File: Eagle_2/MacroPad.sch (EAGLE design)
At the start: 40 parts, among them SW00 SWITCH-SMD-SCHURTER-1241.1612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, SW01 KEYSWITCH-PLAIN-MX-1U, SW02 KEYSWITCH-PLAIN-MX-1U, SW03 KEYSWITCH-PLAIN-MX-1U, SW04 KEYSWITCH-PLAIN-MX-1U, SW05 KEYSWITCH-PLAIN-MX-1U, SW06 KEYSWITCH-PLAIN-MX-1U, SW07 KEYSWITCH-PLAIN-MX-1U, SW08 KEYSWITCH-PLAIN-MX-1U, SW09 KEYSWITCH-PLAIN-MX-1U, SW10 KEYSWITCH-PLAIN-MX-1U, SW11 KEYSWITCH-PLAIN-MX-1U, SW12 KEYSWITCH-PLAIN-MX-1U

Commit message: Create schematic and start aligning pin order
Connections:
- net N$10: now also U$1.PD6(RTS); no longer U$1.PD2(RX)
- net N$16: now also U$1.PD4; no longer U$1.PD0
- net N$26: now also U$1.PD2(RX); no longer U$1.PD4
- net N$32: now also U$1.PD1; no longer U$1.PD5
- net N$38: now also U$1.PD0; no longer U$1.PD6(RTS)
- net N$40: now also U$1.PD5; no longer U$1.PD1
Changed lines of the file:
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@@
 <pinref part="SW01" gate="G$1" pin="P0"/>
 <wire x1="170.18" y1="124.46" x2="172.72" y2="124.46" width="0.1524" layer="91"/>
-<wire x1="172.72" y1="124.46" x2="172.72" y2="137.16" width="0.1524" layer="91"/>
+<wire x1="172.72" y1="124.46" x2="172.72" y2="147.32" width="0.1524" layer="91"/>
 <pinref part="SW04" gate="G$1" pin="P0"/>
 <wire x1="170.18" y1="86.36" x2="172.72" y2="86.36" width="0.1524" layer="91"/>
@@
 <wire x1="172.72" y1="48.26" x2="172.72" y2="10.16" width="0.1524" layer="91"/>
 <junction x="172.72" y="48.26"/>
-<pinref part="U$1" gate="G$1" pin="PD2(RX)"/>
-<wire x1="93.98" y1="55.88" x2="129.54" y2="55.88" width="0.1524" layer="91"/>
-<wire x1="129.54" y1="55.88" x2="129.54" y2="137.16" width="0.1524" layer="91"/>
-<wire x1="129.54" y1="137.16" x2="172.72" y2="137.16" width="0.1524" layer="91"/>
+<pinref part="U$1" gate="G$1" pin="PD6(RTS)"/>
+<wire x1="93.98" y1="45.72" x2="144.78" y2="45.72" width="0.1524" layer="91"/>
+<wire x1="144.78" y1="45.72" x2="144.78" y2="147.32" width="0.1524" layer="91"/>
+<wire x1="144.78" y1="147.32" x2="172.72" y2="147.32" width="0.1524" layer="91"/>
 </segment>
 </net>
@@
 <wire x1="180.34" y1="101.6" x2="157.48" y2="101.6" width="0.1524" layer="91"/>
 <junction x="157.48" y="101.6"/>
-<wire x1="157.48" y1="101.6" x2="132.08" y2="101.6" width="0.1524" layer="91"/>
+<wire x1="157.48" y1="101.6" x2="137.16" y2="101.6" width="0.1524" layer="91"/>
 <junction x="180.34" y="101.6"/>
-<wire x1="132.08" y1="101.6" x2="132.08" y2="53.34" width="0.1524" layer="91"/>
 <pinref part="U$1" gate="G$1" pin="PD3(TX)"/>
-<wire x1="132.08" y1="53.34" x2="93.98" y2="53.34" width="0.1524" layer="91"/>
+<wire x1="93.98" y1="53.34" x2="137.16" y2="53.34" width="0.1524" layer="91"/>
+<wire x1="137.16" y1="53.34" x2="137.16" y2="101.6" width="0.1524" layer="91"/>
 </segment>
 </net>
@@
 <pinref part="SW03" gate="G$1" pin="P0"/>
 <wire x1="215.9" y1="124.46" x2="218.44" y2="124.46" width="0.1524" layer="91"/>
-<wire x1="218.44" y1="124.46" x2="218.44" y2="142.24" width="0.1524" layer="91"/>
+<wire x1="218.44" y1="124.46" x2="218.44" y2="152.4" width="0.1524" layer="91"/>
 <pinref part="SW06" gate="G$1" pin="P0"/>
 <wire x1="215.9" y1="86.36" x2="218.44" y2="86.36" width="0.1524" layer="91"/>
@@
 <wire x1="218.44" y1="48.26" x2="218.44" y2="10.16" width="0.1524" layer="91"/>
 <junction x="218.44" y="48.26"/>
-<pinref part="U$1" gate="G$1" pin="PD0"/>
-<wire x1="93.98" y1="60.96" x2="124.46" y2="60.96" width="0.1524" layer="91"/>
-<wire x1="124.46" y1="60.96" x2="124.46" y2="142.24" width="0.1524" layer="91"/>
-<wire x1="124.46" y1="142.24" x2="218.44" y2="142.24" width="0.1524" layer="91"/>
+<pinref part="U$1" gate="G$1" pin="PD4"/>
+<wire x1="93.98" y1="50.8" x2="139.7" y2="50.8" width="0.1524" layer="91"/>
+<wire x1="139.7" y1="50.8" x2="139.7" y2="152.4" width="0.1524" layer="91"/>
+<wire x1="139.7" y1="152.4" x2="218.44" y2="152.4" width="0.1524" layer="91"/>
 </segment>
 </net>
@@
 <junction x="157.48" y="63.5"/>
 <wire x1="157.48" y1="63.5" x2="134.62" y2="63.5" width="0.1524" layer="91"/>
-<wire x1="134.62" y1="63.5" x2="134.62" y2="50.8" width="0.1524" layer="91"/>
-<pinref part="U$1" gate="G$1" pin="PD4"/>
-<wire x1="134.62" y1="50.8" x2="93.98" y2="50.8" width="0.1524" layer="91"/>
+<wire x1="134.62" y1="63.5" x2="134.62" y2="55.88" width="0.1524" layer="91"/>
+<pinref part="U$1" gate="G$1" pin="PD2(RX)"/>
+<wire x1="134.62" y1="55.88" x2="93.98" y2="55.88" width="0.1524" layer="91"/>
 </segment>
 </net>
@@
 <junction x="157.48" y="25.4"/>
 <wire x1="157.48" y1="25.4" x2="132.08" y2="25.4" width="0.1524" layer="91"/>
-<wire x1="132.08" y1="25.4" x2="132.08" y2="48.26" width="0.1524" layer="91"/>
-<pinref part="U$1" gate="G$1" pin="PD5"/>
-<wire x1="132.08" y1="48.26" x2="93.98" y2="48.26" width="0.1524" layer="91"/>
+<wire x1="132.08" y1="25.4" x2="132.08" y2="58.42" width="0.1524" layer="91"/>
+<pinref part="U$1" gate="G$1" pin="PD1"/>
+<wire x1="132.08" y1="58.42" x2="93.98" y2="58.42" width="0.1524" layer="91"/>
 </segment>
 </net>
@@
 <junction x="180.34" y="-12.7"/>
 <wire x1="157.48" y1="-12.7" x2="129.54" y2="-12.7" width="0.1524" layer="91"/>
-<pinref part="U$1" gate="G$1" pin="PD6(RTS)"/>
-<wire x1="93.98" y1="45.72" x2="129.54" y2="45.72" width="0.1524" layer="91"/>
-<wire x1="129.54" y1="45.72" x2="129.54" y2="-12.7" width="0.1524" layer="91"/>
+<pinref part="U$1" gate="G$1" pin="PD0"/>
+<wire x1="93.98" y1="60.96" x2="129.54" y2="60.96" width="0.1524" layer="91"/>
+<wire x1="129.54" y1="60.96" x2="129.54" y2="-12.7" width="0.1524" layer="91"/>
 </segment>
 </net>
@@
 <pinref part="SW02" gate="G$1" pin="P0"/>
 <wire x1="193.04" y1="124.46" x2="195.58" y2="124.46" width="0.1524" layer="91"/>
-<wire x1="195.58" y1="124.46" x2="195.58" y2="139.7" width="0.1524" layer="91"/>
+<wire x1="195.58" y1="124.46" x2="195.58" y2="149.86" width="0.1524" layer="91"/>
 <pinref part="SW05" gate="G$1" pin="P0"/>
 <wire x1="193.04" y1="86.36" x2="195.58" y2="86.36" width="0.1524" layer="91"/>
@@
 <wire x1="195.58" y1="10.16" x2="195.58" y2="48.26" width="0.1524" layer="91"/>
 <junction x="195.58" y="48.26"/>
-<wire x1="195.58" y1="139.7" x2="127" y2="139.7" width="0.1524" layer="91"/>
-<wire x1="127" y1="139.7" x2="127" y2="58.42" width="0.1524" layer="91"/>
-<pinref part="U$1" gate="G$1" pin="PD1"/>
-<wire x1="127" y1="58.42" x2="93.98" y2="58.42" width="0.1524" layer="91"/>
-</segment>
-</net>
+<wire x1="195.58" y1="149.86" x2="142.24" y2="149.86" width="0.1524" layer="91"/>
+<pinref part="U$1" gate="G$1" pin="PD5"/>
+<wire x1="142.24" y1="149.86" x2="142.24" y2="48.26" width="0.1524" layer="91"/>
+<wire x1="142.24" y1="48.26" x2="93.98" y2="48.26" width="0.1524" layer="91"/>
+</segment>
+</net>

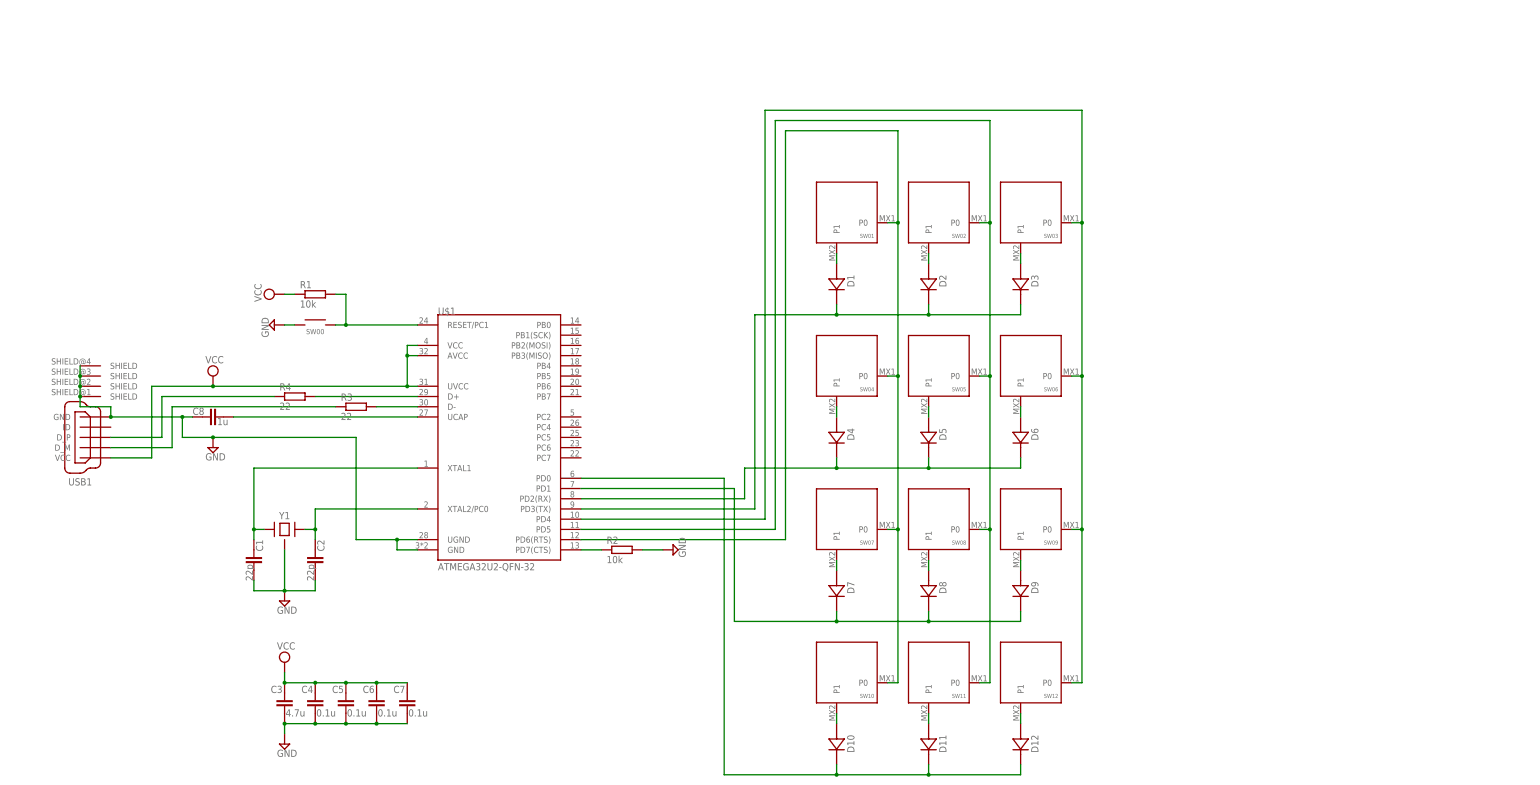
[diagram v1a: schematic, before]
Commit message: Update switch and chip footprints, and switch array pins
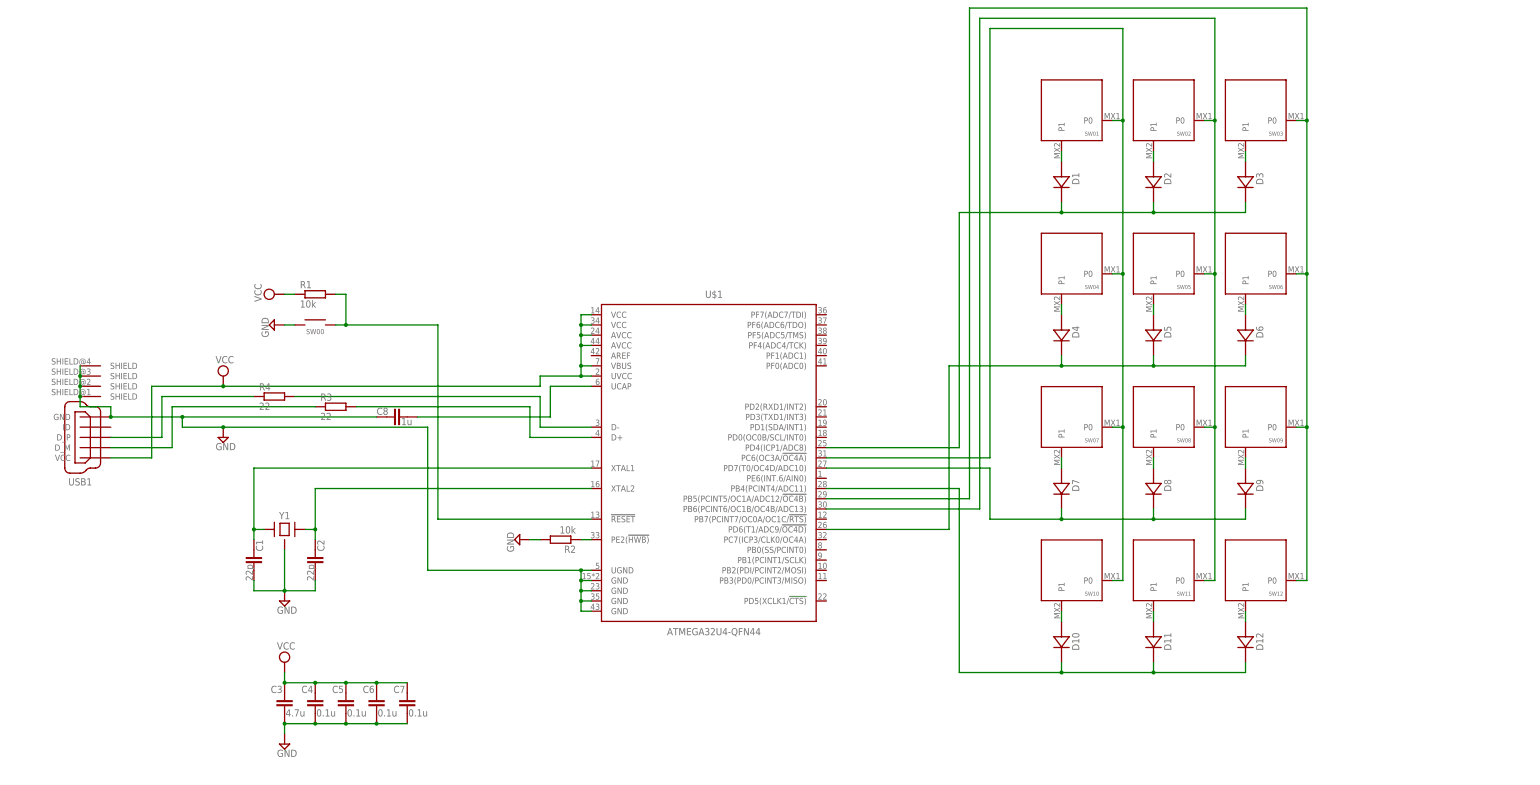
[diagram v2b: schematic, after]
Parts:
- SW00: value SWITCH-SMD-SCHURTER-1241.1612.11 -> SWITCH-SMD-EVQP-P2602W; device Hardware:SWITCH-SMD-SCHURTER-1241.1612.11 -> Hardware:SWITCH-SMD-EVQP-P2602W
- U$1: value ATMEGA32U2-QFN-32 -> ATMEGA32U4-QFN44; device Controller:ATMEGA32U2-QFN-32 -> Controller:ATMEGA32U4-QFN44
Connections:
- net GND: now also R2.2, U$1.GND@15, U$1.GND@23, U$1.GND@35, U$1.GND@43; no longer U$1.GND
- net N$1: now also U$1.XTAL2; no longer U$1.XTAL2/PC0
- net N$10: now also U$1.PC6(OC3A/!OC4A); no longer U$1.PD6(RTS)
- net N$14: now also U$1.PD4(ICP1/ADC8); no longer U$1.PD3(TX)
- net N$16: now also U$1.PB5(PCINT5/OC1A/ADC12/!OC4B); no longer U$1.PD4
- net N$26: now also U$1.PD6(T1/ADC9/!OC4D); no longer U$1.PD2(RX)
- net N$3: now also U$1.!RESET; no longer U$1.RESET/PC1
- net N$32: now also U$1.PD7(T0/OC4D/ADC10); no longer U$1.PD1
- net N$38: now also U$1.PB4(PCINT4/ADC11); no longer U$1.PD0
- net N$4: now also U$1.PE2(!HWB); no longer U$1.PD7(CTS)
- net N$40: now also U$1.PB6(PCINT6/OC1B/OC4B/ADC13); no longer U$1.PD5
- net N$6: now also U$1.D-; no longer U$1.D+
- net N$8: now also U$1.D+; no longer U$1.D-
- net UGND: no longer R2.2
- net VCC: now also U$1.AVCC@24, U$1.AVCC@44, U$1.VBUS, U$1.VCC@14, U$1.VCC@34; no longer U$1.AVCC, U$1.VCC
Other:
- moved on the sheet: C8, D1, D10, D11, D12, D2, D3, D4, D5, D6, D7, D8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

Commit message: Routed board
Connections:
- removed net GND: C8.1, R2.2, U$1.GND@15, U$1.GND@23, U$1.GND@35, U$1.GND@43, U$1.UGND, USB1.GND, USB1.SHIELD@1, USB1.SHIELD@2, USB1.SHIELD@3, USB1.SHIELD@4
- net UGND: now also C8.1, R2.2, U$1.GND@15, U$1.GND@23, U$1.GND@35, U$1.GND@43, U$1.UGND, USB1.GND, USB1.SHIELD@1, USB1.SHIELD@2, USB1.SHIELD@3, USB1.SHIELD@4
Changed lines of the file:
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@@
 <part name="U$1" library="Controller" deviceset="ATMEGA32U4" device="-QFN44"/>
 <part name="SW00" library="Hardware" deviceset="SWITCH-SMD" device="-EVQP-P2602W"/>
+<part name="SUPPLY9" library="supply2" library_urn="urn:adsk.eagle:library:372" deviceset="GND" device=""/>
 </parts>
 <sheets>
@@
 <instance part="SW00" gate="G$1" x="27.94" y="99.06" smashed="yes">
 <attribute name="NAME" x="27.94" y="96.774" size="1.27" layer="95" align="bottom-center"/>
+</instance>
+<instance part="SUPPLY9" gate="GND" x="66.04" y="17.78" smashed="yes">
+<attribute name="VALUE" x="64.135" y="14.605" size="1.778" layer="96"/>
 </instance>
 </instances>
@@
 <wire x1="20.32" y1="99.06" x2="22.86" y2="99.06" width="0.1524" layer="91"/>
 <pinref part="SW00" gate="G$1" pin="1"/>
+</segment>
+<segment>
+<pinref part="SUPPLY6" gate="GND" pin="GND"/>
+<pinref part="R2" gate="G$1" pin="2"/>
+<wire x1="81.28" y1="45.72" x2="83.82" y2="45.72" width="0.1524" layer="91"/>
+</segment>
+<segment>
+<pinref part="USB1" gate="G$1" pin="GND"/>
+<wire x1="-22.86" y1="76.2" x2="-5.08" y2="76.2" width="0.1524" layer="91"/>
+<wire x1="-5.08" y1="76.2" x2="43.18" y2="76.2" width="0.1524" layer="91"/>
+<wire x1="-22.86" y1="76.2" x2="-22.86" y2="78.74" width="0.1524" layer="91"/>
+<junction x="-22.86" y="76.2"/>
+<pinref part="USB1" gate="G$1" pin="SHIELD@2"/>
+<pinref part="USB1" gate="G$1" pin="SHIELD@1"/>
+<wire x1="-30.48" y1="83.82" x2="-30.48" y2="81.28" width="0.1524" layer="91"/>
+<pinref part="USB1" gate="G$1" pin="SHIELD@4"/>
+<pinref part="USB1" gate="G$1" pin="SHIELD@3"/>
+<wire x1="-30.48" y1="88.9" x2="-30.48" y2="86.36" width="0.1524" layer="91"/>
+<wire x1="-30.48" y1="83.82" x2="-30.48" y2="86.36" width="0.1524" layer="91"/>
+<junction x="-30.48" y="83.82"/>
+<junction x="-30.48" y="86.36"/>
+<wire x1="-22.86" y1="78.74" x2="-30.48" y2="78.74" width="0.1524" layer="91"/>
+<wire x1="-30.48" y1="78.74" x2="-30.48" y2="81.28" width="0.1524" layer="91"/>
+<junction x="-30.48" y="81.28"/>
+<pinref part="C8" gate="G$1" pin="1"/>
+<wire x1="-5.08" y1="76.2" x2="-5.08" y2="73.66" width="0.1524" layer="91"/>
+<junction x="-5.08" y="76.2"/>
+<wire x1="-5.08" y1="73.66" x2="5.08" y2="73.66" width="0.1524" layer="91"/>
+<wire x1="5.08" y1="73.66" x2="55.88" y2="73.66" width="0.1524" layer="91"/>
+<pinref part="SUPPLY7" gate="GND" pin="GND"/>
+<junction x="5.08" y="73.66"/>
+<pinref part="U$1" gate="G$1" pin="GND@43"/>
+<wire x1="96.52" y1="27.94" x2="93.98" y2="27.94" width="0.1524" layer="91"/>
+<wire x1="93.98" y1="27.94" x2="93.98" y2="30.48" width="0.1524" layer="91"/>
+<pinref part="U$1" gate="G$1" pin="GND@35"/>
+<wire x1="96.52" y1="30.48" x2="93.98" y2="30.48" width="0.1524" layer="91"/>
+<junction x="93.98" y="30.48"/>
+<wire x1="93.98" y1="30.48" x2="93.98" y2="33.02" width="0.1524" layer="91"/>
+<pinref part="U$1" gate="G$1" pin="GND@23"/>
+<wire x1="96.52" y1="33.02" x2="93.98" y2="33.02" width="0.1524" layer="91"/>
+<junction x="93.98" y="33.02"/>
+<wire x1="93.98" y1="33.02" x2="93.98" y2="35.56" width="0.1524" layer="91"/>
+<pinref part="U$1" gate="G$1" pin="GND@15"/>
+<wire x1="96.52" y1="35.56" x2="93.98" y2="35.56" width="0.1524" layer="91"/>
+<junction x="93.98" y="35.56"/>
+<wire x1="93.98" y1="35.56" x2="93.98" y2="38.1" width="0.1524" layer="91"/>
+<wire x1="93.98" y1="38.1" x2="55.88" y2="38.1" width="0.1524" layer="91"/>
+<wire x1="55.88" y1="73.66" x2="55.88" y2="38.1" width="0.1524" layer="91"/>
+<pinref part="U$1" gate="G$1" pin="UGND"/>
+<wire x1="96.52" y1="38.1" x2="93.98" y2="38.1" width="0.1524" layer="91"/>
+<junction x="93.98" y="38.1"/>
+</segment>
+<segment>
+<pinref part="SUPPLY9" gate="GND" pin="GND"/>
+<wire x1="66.04" y1="20.32" x2="66.04" y2="27.94" width="0.1524" layer="91"/>
+<label x="66.04" y="27.94" size="1.778" layer="95" xref="yes"/>
 </segment>
 </net>
@@
 </segment>
 </net>
-<net name="GND" class="0">
-<segment>
-<pinref part="USB1" gate="G$1" pin="GND"/>
-<wire x1="-22.86" y1="76.2" x2="-5.08" y2="76.2" width="0.1524" layer="91"/>
-<wire x1="-5.08" y1="76.2" x2="43.18" y2="76.2" width="0.1524" layer="91"/>
-<wire x1="-22.86" y1="76.2" x2="-22.86" y2="78.74" width="0.1524" layer="91"/>
-<junction x="-22.86" y="76.2"/>
-<pinref part="USB1" gate="G$1" pin="SHIELD@2"/>
-<pinref part="USB1" gate="G$1" pin="SHIELD@1"/>
-<wire x1="-30.48" y1="83.82" x2="-30.48" y2="81.28" width="0.1524" layer="91"/>
-<pinref part="USB1" gate="G$1" pin="SHIELD@4"/>
-<pinref part="USB1" gate="G$1" pin="SHIELD@3"/>
-<wire x1="-30.48" y1="88.9" x2="-30.48" y2="86.36" width="0.1524" layer="91"/>
-<wire x1="-30.48" y1="83.82" x2="-30.48" y2="86.36" width="0.1524" layer="91"/>
-<junction x="-30.48" y="83.82"/>
-<junction x="-30.48" y="86.36"/>
-<wire x1="-22.86" y1="78.74" x2="-30.48" y2="78.74" width="0.1524" layer="91"/>
-<wire x1="-30.48" y1="78.74" x2="-30.48" y2="81.28" width="0.1524" layer="91"/>
-<junction x="-30.48" y="81.28"/>
-<pinref part="C8" gate="G$1" pin="1"/>
-<wire x1="-5.08" y1="76.2" x2="-5.08" y2="73.66" width="0.1524" layer="91"/>
-<junction x="-5.08" y="76.2"/>
-<wire x1="-5.08" y1="73.66" x2="5.08" y2="73.66" width="0.1524" layer="91"/>
-<wire x1="5.08" y1="73.66" x2="55.88" y2="73.66" width="0.1524" layer="91"/>
-<pinref part="SUPPLY7" gate="GND" pin="GND"/>
-<junction x="5.08" y="73.66"/>
-<pinref part="U$1" gate="G$1" pin="UGND"/>
-<wire x1="96.52" y1="38.1" x2="93.98" y2="38.1" width="0.1524" layer="91"/>
-<junction x="93.98" y="38.1"/>
-<pinref part="U$1" gate="G$1" pin="GND@43"/>
-<wire x1="96.52" y1="27.94" x2="93.98" y2="27.94" width="0.1524" layer="91"/>
-<wire x1="93.98" y1="27.94" x2="93.98" y2="30.48" width="0.1524" layer="91"/>
-<pinref part="U$1" gate="G$1" pin="GND@35"/>
-<wire x1="96.52" y1="30.48" x2="93.98" y2="30.48" width="0.1524" layer="91"/>
-<junction x="93.98" y="30.48"/>
-<wire x1="93.98" y1="30.48" x2="93.98" y2="33.02" width="0.1524" layer="91"/>
-<pinref part="U$1" gate="G$1" pin="GND@23"/>
-<wire x1="96.52" y1="33.02" x2="93.98" y2="33.02" width="0.1524" layer="91"/>
-<junction x="93.98" y="33.02"/>
-<wire x1="93.98" y1="33.02" x2="93.98" y2="35.56" width="0.1524" layer="91"/>
-<pinref part="U$1" gate="G$1" pin="GND@15"/>
-<wire x1="96.52" y1="35.56" x2="93.98" y2="35.56" width="0.1524" layer="91"/>
-<junction x="93.98" y="35.56"/>
-<wire x1="93.98" y1="35.56" x2="93.98" y2="38.1" width="0.1524" layer="91"/>
-<wire x1="93.98" y1="38.1" x2="55.88" y2="38.1" width="0.1524" layer="91"/>
-<wire x1="55.88" y1="73.66" x2="55.88" y2="38.1" width="0.1524" layer="91"/>
-</segment>
-<segment>
-<pinref part="SUPPLY6" gate="GND" pin="GND"/>
-<pinref part="R2" gate="G$1" pin="2"/>
-<wire x1="81.28" y1="45.72" x2="83.82" y2="45.72" width="0.1524" layer="91"/>
-</segment>
-</net>

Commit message: Components routed in compressed area
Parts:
- added U$2: KEYSWITCH-PLAIN-MX-1U, Keyboard:KEYSWITCH-PLAIN-MX-1U
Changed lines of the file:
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@@
 <part name="SW00" library="Hardware" deviceset="SWITCH-SMD" device="-EVQP-P2602W"/>
 <part name="SUPPLY9" library="supply2" library_urn="urn:adsk.eagle:library:372" deviceset="GND" device=""/>
+<part name="U$2" library="Keyboard" deviceset="KEYSWITCH-PLAIN" device="-MX-1U"/>
 </parts>
 <sheets>
@@
 <attribute name="VALUE" x="64.135" y="14.605" size="1.778" layer="96"/>
 </instance>
+<instance part="U$2" gate="G$1" x="322.58" y="30.48" smashed="yes">
+<attribute name="NAME" x="315.77" y="35.798" size="1" layer="95"/>
+</instance>
 </instances>

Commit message: Shrink board
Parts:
- removed U$2: KEYSWITCH-PLAIN-MX-1U, Keyboard:KEYSWITCH-PLAIN-MX-1U
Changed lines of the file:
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@@
 <part name="SW00" library="Hardware" deviceset="SWITCH-SMD" device="-EVQP-P2602W"/>
 <part name="SUPPLY9" library="supply2" library_urn="urn:adsk.eagle:library:372" deviceset="GND" device=""/>
-<part name="U$2" library="Keyboard" deviceset="KEYSWITCH-PLAIN" device="-MX-1U"/>
 </parts>
 <sheets>
@@
 <attribute name="VALUE" x="64.135" y="14.605" size="1.778" layer="96"/>
 </instance>
-<instance part="U$2" gate="G$1" x="322.58" y="30.48" smashed="yes">
-<attribute name="NAME" x="315.77" y="35.798" size="1" layer="95"/>
-</instance>
 </instances>
